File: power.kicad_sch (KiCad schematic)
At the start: 20 parts, among them IC2 NCV317BD2TR4G, U3 TPS73601DBV, U4 TPS73601DBV

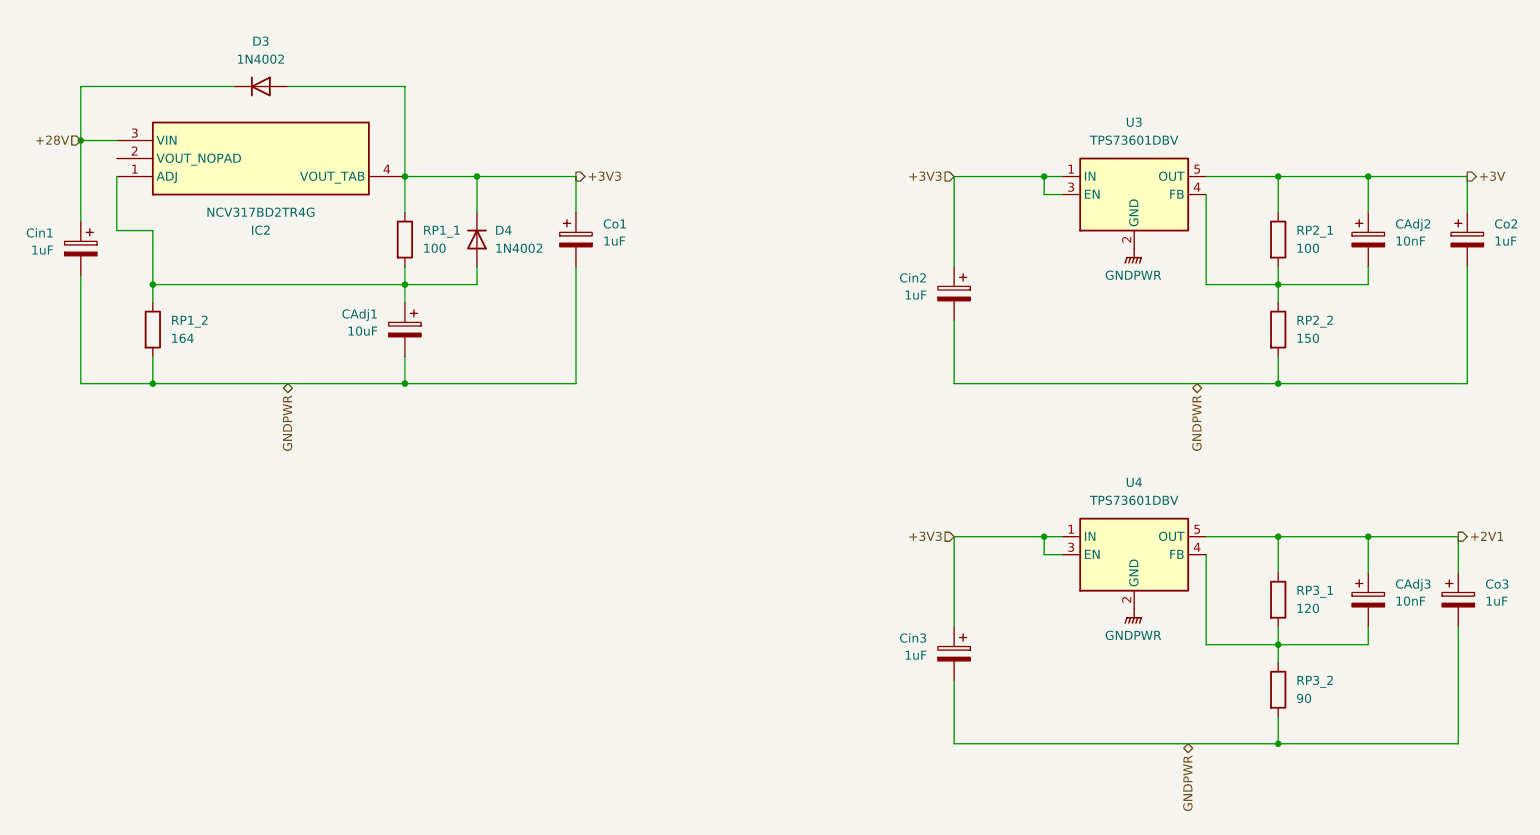
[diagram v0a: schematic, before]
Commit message: Added lots more connections
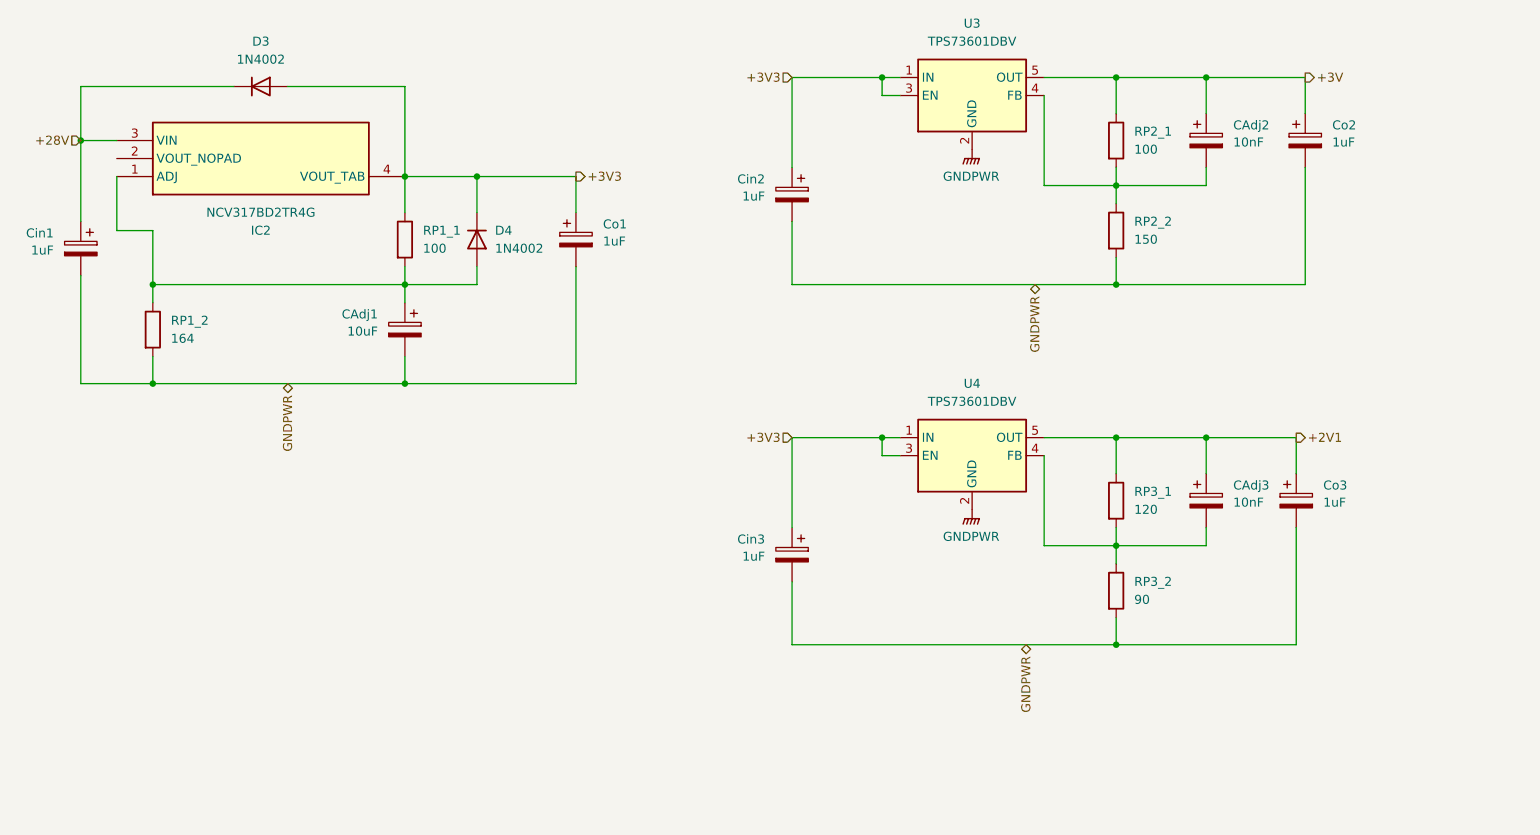
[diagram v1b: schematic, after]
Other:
- moved on the sheet: CAdj2, CAdj3, Cin2, Cin3, Co2, Co3, RP2_1, RP2_2, RP3_1, RP3_2, U3, U4
